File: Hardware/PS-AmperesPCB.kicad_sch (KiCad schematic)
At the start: 10 parts, among them J1 PeripheralCAN, J2 PeripheralCAN

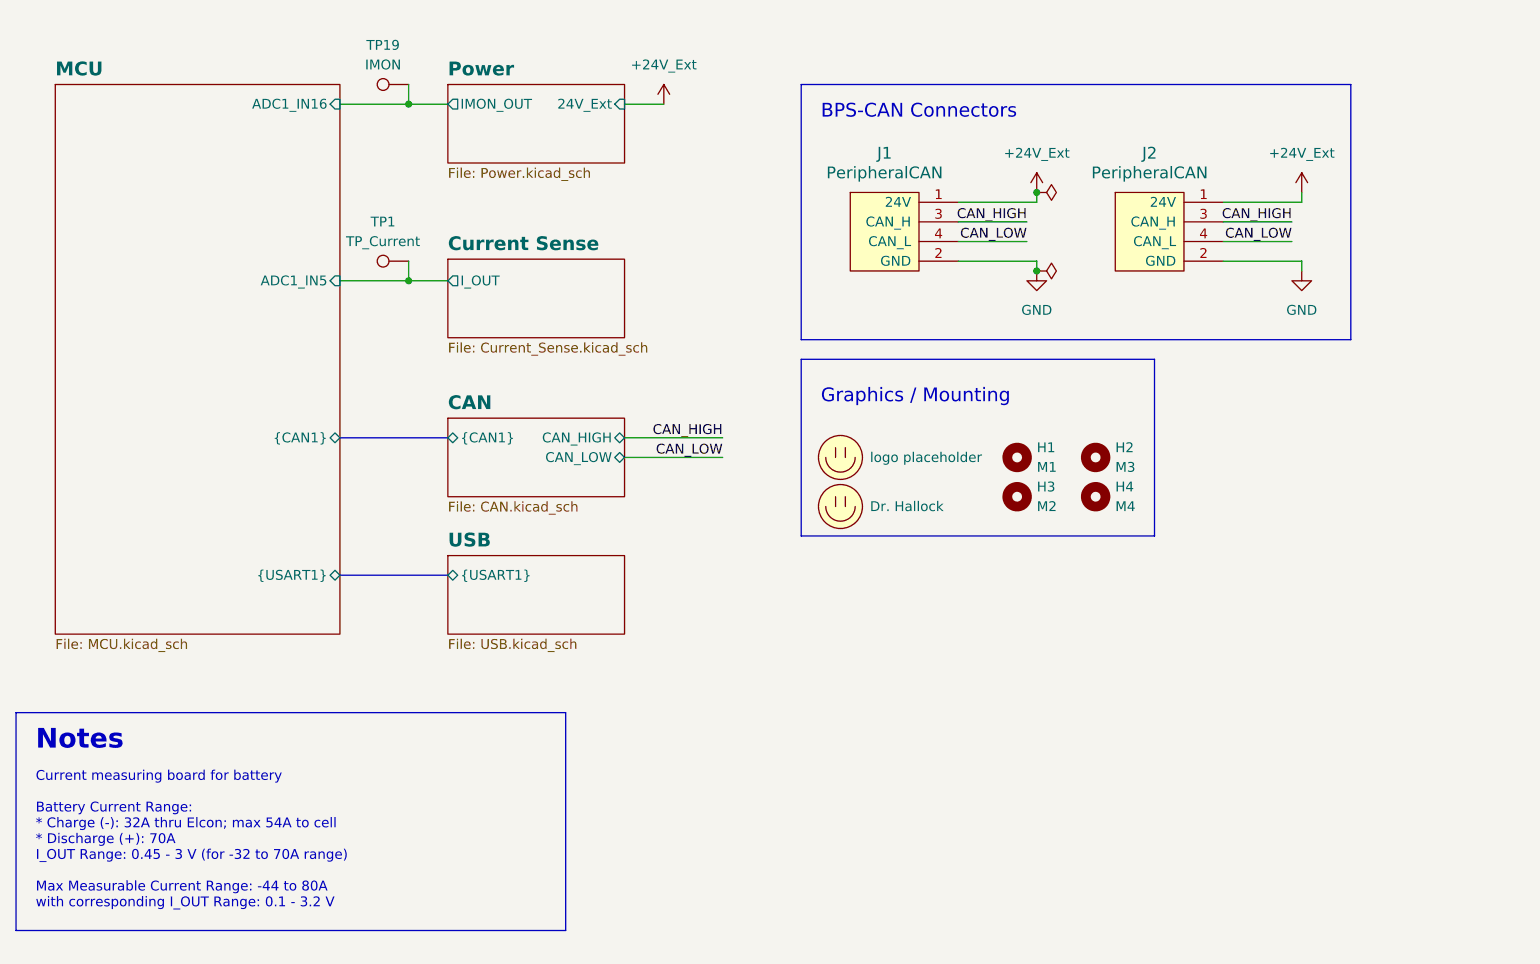
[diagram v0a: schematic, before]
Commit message: RevB Changes (#4)
* added documentation for current range; added VBUS led

* INA common-mode fixed (i think)

* differential amp for LPF

* diff amp / LPF

* some comments so I don't forget what I'm doing

* new TLV symbol, SPDT switch for scrut

* fixed LPF cutoff

* refactored and added LPF docs; added fuse, boot_gpio from USB-UART chip

* i lowk haven't started layout

* slightly cooked

* started layout not really but kind of

* layout stuff

* post review council sch changes: shielded connectors, removed SHDN resistor, diode OR for boot, standardized resistors

* starting routing i think

* almost done with routing

* wow

* drc is happy

* ye

* again

* addressed some comments

* added lcsc part numbers

* generated production files and docs

* updated STEP file

* symbol library

* addressed comments; generated production files, docs

* added Mouser BOM, deleted embedded step files
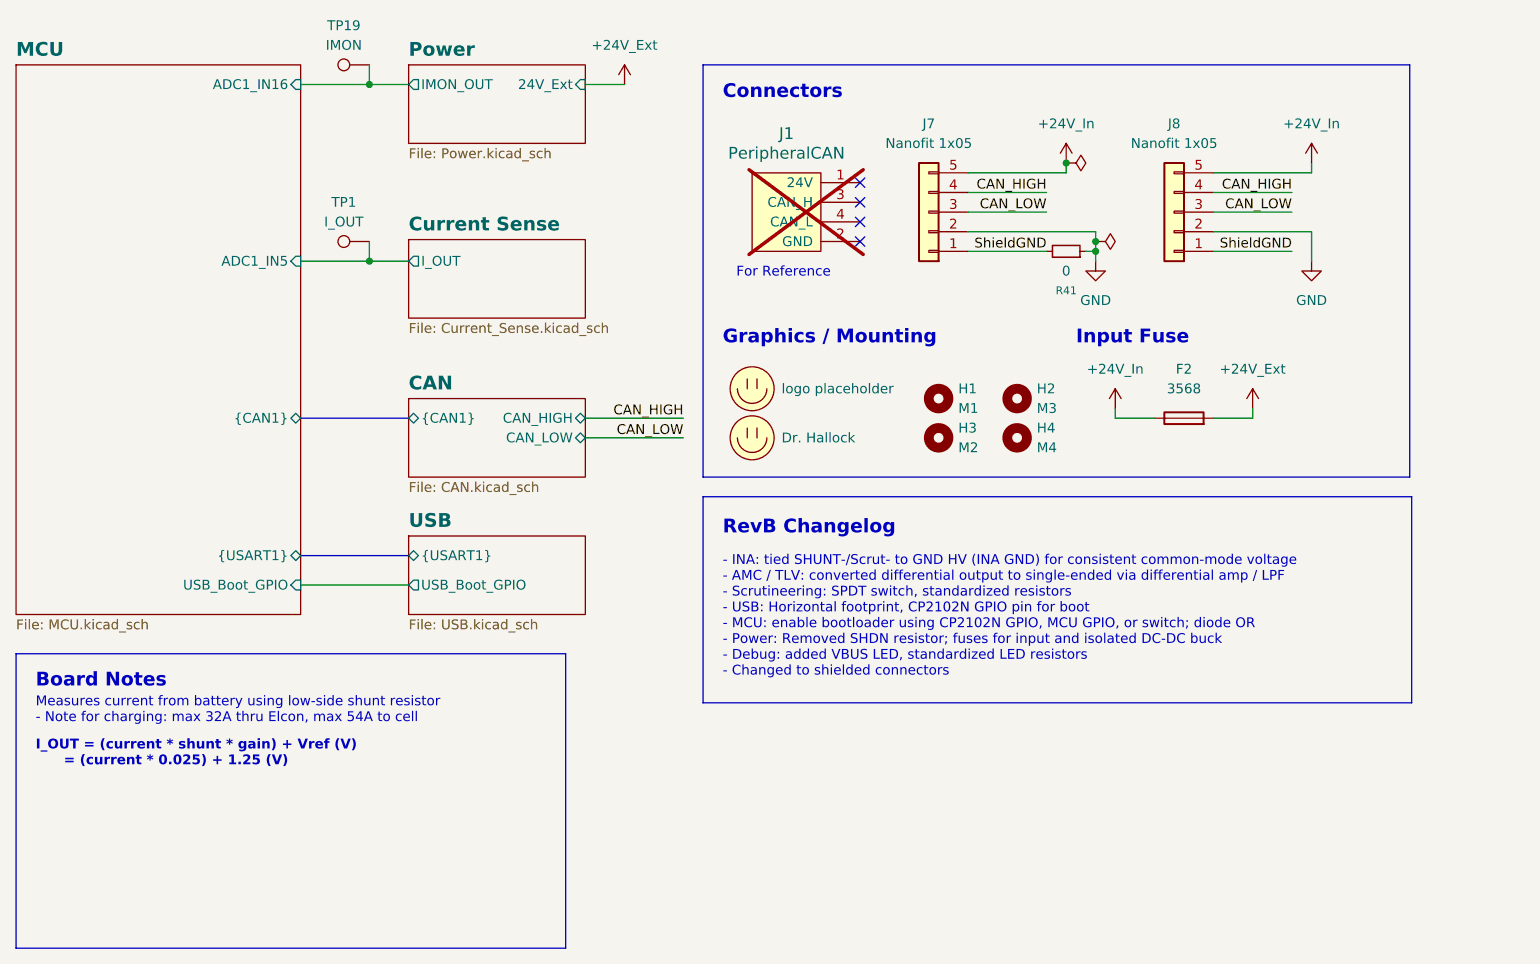
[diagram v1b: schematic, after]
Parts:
- removed J2: PeripheralCAN, UTSVT_Connectors:Molex_Nano-Fit_105309-xx04_1x04_P2.50mm_Vertical, symbol utsvt-connectors:PeripheralCANConnector
- added F2: 3568, Parts:FUSE_3568, symbol Device:Fuse
- added J7, J8: Nanofit 1x05, Connector_Molex:Molex_Nano-Fit_105309-xx05_1x05_P2.50mm_Vertical, symbol Connector_Generic:Conn_01x05
- added R41: 0, Resistor_SMD:R_0603_1608Metric_Pad0.98x0.95mm_HandSolder, symbol Device:R_Small
- J1: now not fitted; now left out of the parts list
- LOGO1, LOGO2: now left out of the parts list
- TP1: value TP_Current -> I_OUT; footprint TestPoint:TestPoint_Keystone_5005-5009_Compact -> Connector_PinHeader_2.54mm:PinHeader_1x01_P2.54mm_Vertical
- TP19: footprint TestPoint:TestPoint_Keystone_5005-5009_Compact -> TestPoint:TestPoint_Pad_1.0x1.0mm; now left out of the parts list
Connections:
- net +24V_Ext: now also F2.2; no longer J1.1 (24V)
- net CAN_HIGH: now also J7.4 (Pin_4), J8.4 (Pin_4); no longer J1.3 (CAN_H)
- net CAN_LOW: now also J7.3 (Pin_3), J8.3 (Pin_3); no longer J1.4 (CAN_L)
- net GND: now also J7.2 (Pin_2), J8.2 (Pin_2), R41.1; no longer J1.2 (GND)
- new net +24V_In: F2.1, J7.5 (Pin_5), J8.5 (Pin_5)
- new net ShieldGND: J7.1 (Pin_1), J8.1 (Pin_1), R41.2
- no-connect marks 0 -> 4
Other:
- sheet MCU ports: added USB_Boot_GPIO; removed none
- sheet USB ports: added USB_Boot_GPIO; removed none
- note added: "- INA: tied SHUNT-/Scrut- to GND HV (INA GND) for consistent common-mode voltage - AMC / TLV: converted differential output to single-ended via differential amp / LPF - Scrutineering: SPDT switch, standardized resistors - USB: Horizontal footprint, CP2102N GPIO pin for boot - MCU: enable bootloader using CP2102N GPIO, MCU GPIO, or switch; diode OR - Power: Removed SHDN resistor; fuses for input a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"
- note added: "Board Notes"
- note added: "Connectors"
- note added: "For Reference"
- note added: "I_OUT = (current * shunt * gain) + Vref (V) = (current * 0.025) + 1.25 (V)"
- note added: "Input Fuse"
- note added: "Measures current from battery using low-side shunt resistor - Note for charging: max 32A thru Elcon, max 54A to cell"
- note added: "RevB Changelog"
- note removed: "BPS-CAN Connectors"
- note removed: "Current measuring board for battery Battery Current Range: * Charge (-): 32A thru Elcon; max 54A to cell * Discharge (+): 70A I_OUT Range: 0.45 - 3 V (for -32 to 70A range) Max Measurable Current Range: -44 to 80A with corresponding I_OUT Range: 0.1 - 3.2 V"
- note removed: "Notes"
- moved on the sheet: H1, H2, H3, H4, TP1, TP19
